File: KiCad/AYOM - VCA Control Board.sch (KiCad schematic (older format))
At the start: 11 parts, among them J1 SIGNAL_OUT, J2 CV1, J3 CV2, J4 SIGNAL_IN, J5 CONN_1, J6 CONN_2, SW1 SW_SPDT

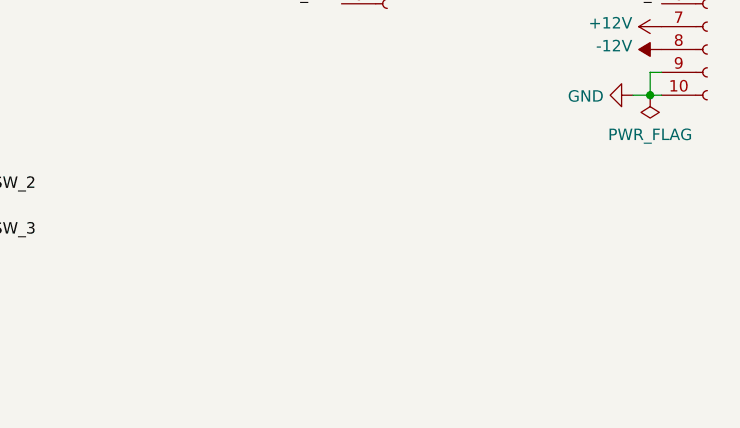
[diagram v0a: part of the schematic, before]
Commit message: Updated acronyms in filenames
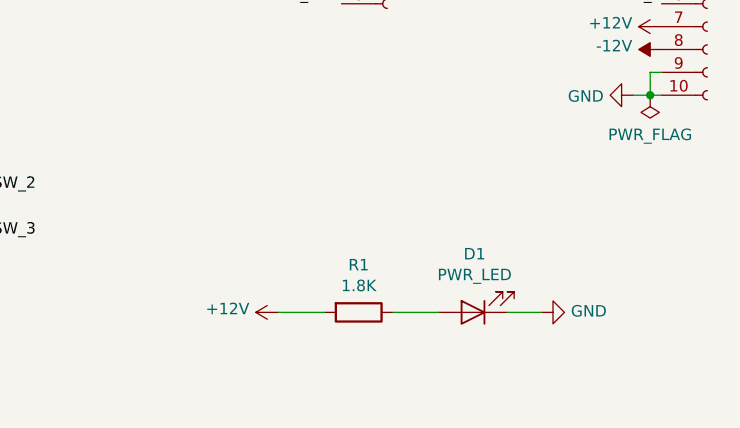
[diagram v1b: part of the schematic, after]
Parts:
- added D1: PWR_LED, LED_THT:LED_D3.0mm, symbol Device:LED
- added R1: 1.8K, Resistor_THT:R_Axial_DIN0207_L6.3mm_D2.5mm_P7.62mm_Horizontal, symbol Device:R
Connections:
- net +12V: now also R1.2
- net GND: now also D1.1 (K)
- new net: D1.2 (A), R1.1
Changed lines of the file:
@@
 TRIM_3
 $Comp
-L power:+12V #PWR0101
+L power:+12V #PWR013
 U 1 1 5EC4064E
 P 8900 2975
-F 0 "#PWR0101" H 8900 2825 50  0001 C CNN
+F 0 "#PWR013" H 8900 2825 50  0001 C CNN
 F 1 "+12V" V 8915 3103 50  0000 L CNN
 F 2 "" H 8900 2975 50  0001 C CNN
@@
 $EndComp
 $Comp
-L power:-12V #PWR0102
+L power:-12V #PWR014
 U 1 1 5EC40B61
 P 8900 3075
-F 0 "#PWR0102" H 8900 3175 50  0001 C CNN
+F 0 "#PWR014" H 8900 3175 50  0001 C CNN
 F 1 "-12V" V 8915 3203 50  0000 L CNN
 F 2 "" H 8900 3075 50  0001 C CNN
@@
 $EndComp
 $Comp
-L power:GND #PWR0103
+L power:GND #PWR012
 U 1 1 5EC40DB7
 P 8775 3275
-F 0 "#PWR0103" H 8775 3025 50  0001 C CNN
+F 0 "#PWR012" H 8775 3025 50  0001 C CNN
 F 1 "GND" V 8780 3147 50  0000 R CNN
 F 2 "" H 8775 3275 50  0001 C CNN
@@
 $EndComp
 $Comp
-L power:+12V #PWR0104
+L power:+12V #PWR06
 U 1 1 5EC49653
 P 3775 1525
-F 0 "#PWR0104" H 3775 1375 50  0001 C CNN
+F 0 "#PWR06" H 3775 1375 50  0001 C CNN
 F 1 "+12V" H 3790 1698 50  0000 C CNN
 F 2 "" H 3775 1525 50  0001 C CNN
@@
 $EndComp
 $Comp
-L power:-12V #PWR0105
+L power:-12V #PWR07
 U 1 1 5EC4988F
 P 3775 2575
-F 0 "#PWR0105" H 3775 2675 50  0001 C CNN
+F 0 "#PWR07" H 3775 2675 50  0001 C CNN
 F 1 "-12V" H 3790 2748 50  0000 C CNN
 F 2 "" H 3775 2575 50  0001 C CNN
@@
 $EndComp
 $Comp
-L power:GND #PWR0106
+L power:GND #PWR01
 U 1 1 5EC51CC3
 P 2175 2000
-F 0 "#PWR0106" H 2175 1750 50  0001 C CNN
+F 0 "#PWR01" H 2175 1750 50  0001 C CNN
 F 1 "GND" H 2180 1827 50  0000 C CNN
 F 2 "" H 2175 2000 50  0001 C CNN
@@
 $EndComp
 $Comp
-L power:GND #PWR0107
+L power:GND #PWR02
 U 1 1 5EC52690
 P 2175 2775
-F 0 "#PWR0107" H 2175 2525 50  0001 C CNN
+F 0 "#PWR02" H 2175 2525 50  0001 C CNN
 F 1 "GND" H 2180 2602 50  0000 C CNN
 F 2 "" H 2175 2775 50  0001 C CNN
@@
 CV2
 $Comp
-L power:GND #PWR0108
+L power:GND #PWR03
 U 1 1 5EC54372
 P 2175 3575
-F 0 "#PWR0108" H 2175 3325 50  0001 C CNN
+F 0 "#PWR03" H 2175 3325 50  0001 C CNN
 F 1 "GND" H 2180 3402 50  0000 C CNN
 F 2 "" H 2175 3575 50  0001 C CNN
@@
 SIGNAL_IN
 $Comp
-L power:GND #PWR0109
+L power:GND #PWR04
 U 1 1 5EC56D21
 P 2550 4425
-F 0 "#PWR0109" H 2550 4175 50  0001 C CNN
+F 0 "#PWR04" H 2550 4175 50  0001 C CNN
 F 1 "GND" H 2555 4252 50  0000 C CNN
 F 2 "" H 2550 4425 50  0001 C CNN
@@
 SIGNAL_OUT
 $Comp
-L power:+12V #PWR0110
+L power:+12V #PWR08
 U 1 1 5EC59CEA
 P 5025 1500
-F 0 "#PWR0110" H 5025 1350 50  0001 C CNN
+F 0 "#PWR08" H 5025 1350 50  0001 C CNN
 F 1 "+12V" H 5040 1673 50  0000 C CNN
 F 2 "" H 5025 1500 50  0001 C CNN
@@
 $EndComp
 $Comp
-L power:-12V #PWR0111
+L power:-12V #PWR09
 U 1 1 5EC5A3FE
 P 5025 2575
-F 0 "#PWR0111" H 5025 2675 50  0001 C CNN
+F 0 "#PWR09" H 5025 2675 50  0001 C CNN
 F 1 "-12V" H 5040 2748 50  0000 C CNN
 F 2 "" H 5025 2575 50  0001 C CNN
@@
 OFFSET_ADJ
 $Comp
-L power:GND #PWR0112
+L power:GND #PWR05
 U 1 1 5EC935CF
 P 3625 3200
-F 0 "#PWR0112" H 3625 2950 50  0001 C CNN
+F 0 "#PWR05" H 3625 2950 50  0001 C CNN
 F 1 "GND" H 3630 3027 50  0000 C CNN
 F 2 "" H 3625 3200 50  0001 C CNN
@@
 NoConn ~ 2575 3350
 NoConn ~ 2150 4200
+$Comp
+L Device:R R1
+U 1 1 5F7669BF
+P 7575 4225
+F 0 "R1" V 7368 4225 50  0000 C CNN
+F 1 "1.8K" V 7459 4225 50  0000 C CNN
+F 2 "Resistor_THT:R_Axial_DIN0207_L6.3mm_D2.5mm_P7.62mm_Horizontal" V 7505 4225 50  0001 C CNN
+F 3 "~" H 7575 4225 50  0001 C CNN
+	1    7575 4225
+	0    1    1    0
+$EndComp
+$Comp
+L power:+12V #PWR010
+U 1 1 5F7673A3
+P 7225 4225
+F 0 "#PWR010" H 7225 4075 50  0001 C CNN
+F 1 "+12V" V 7240 4353 50  0000 L CNN
+F 2 "" H 7225 4225 50  0001 C CNN
+F 3 "" H 7225 4225 50  0001 C CNN
+	1    7225 4225
+	0    -1   -1   0
+$EndComp
+Wire Wire Line
+	7225 4225 7425 4225
+$Comp
+L Device:LED D1
+U 1 1 5F76830F
+P 8075 4225
+F 0 "D1" H 8068 3970 50  0000 C CNN
+F 1 "PWR_LED" H 8068 4061 50  0000 C CNN
+F 2 "LED_THT:LED_D3.0mm" H 8075 4225 50  0001 C CNN
+F 3 "~" H 8075 4225 50  0001 C CNN
+	1    8075 4225
+	-1   0    0    1
+$EndComp
+Wire Wire Line
+	7925 4225 7725 4225
+$Comp
+L power:GND #PWR011
+U 1 1 5F768F37
+P 8375 4225
+F 0 "#PWR011" H 8375 3975 50  0001 C CNN
+F 1 "GND" V 8380 4097 50  0000 R CNN
+F 2 "" H 8375 4225 50  0001 C CNN
+F 3 "" H 8375 4225 50  0001 C CNN
+	1    8375 4225
+	0    -1   -1   0
+$EndComp
+Wire Wire Line
+	8225 4225 8375 4225
 $EndSCHEMATC
